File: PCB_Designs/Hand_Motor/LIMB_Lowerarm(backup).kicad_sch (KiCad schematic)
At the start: 18 parts, among them J1 Power In, J10 68800311622, J11 Servo Power, J12 68800611722, J13 68800611722, J2 IMU, J3 CAN IN, J4 CAN OUT, J5 68800311622, J6 68800311622, J7 68800311622, J8 68800311622, J9 68800311622, U1 ESP32-C3-Zero, U3 SN65HVD230

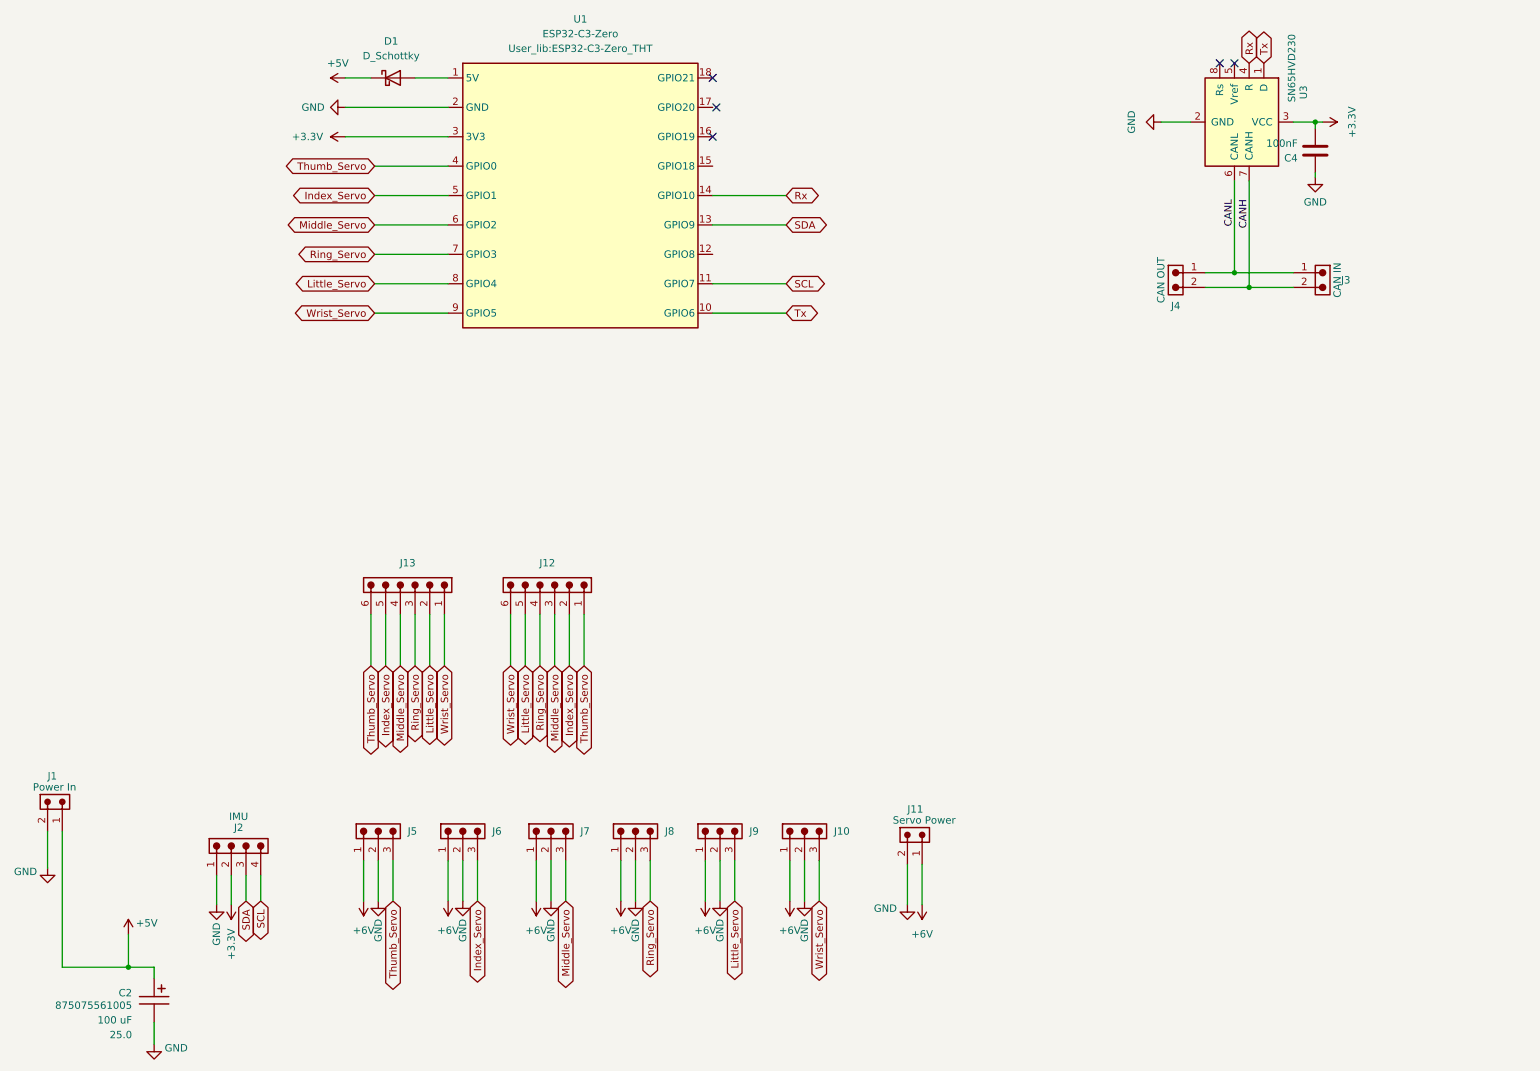
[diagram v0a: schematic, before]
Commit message: PCB kort
Uppdaterat Hand Pressure och Motor korten
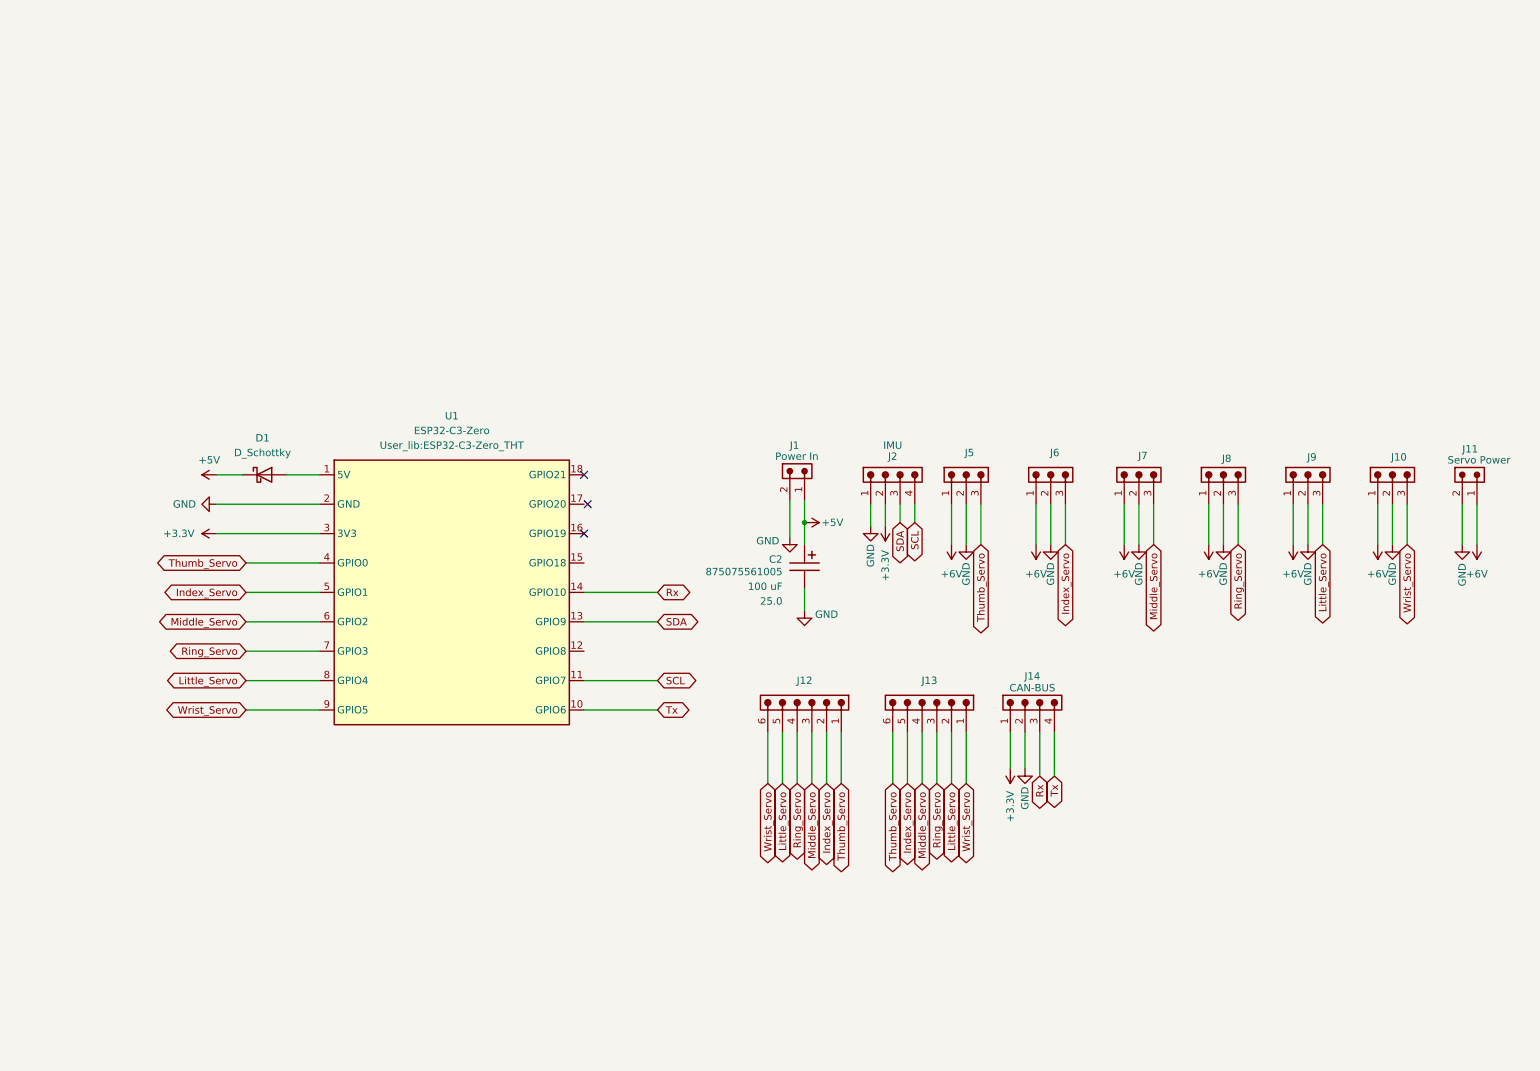
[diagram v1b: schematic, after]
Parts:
- removed C4: 100nF, Capacitor_SMD:C_0805_2012Metric_Pad1.18x1.45mm_HandSolder, symbol Device:C
- removed J3: CAN IN, Connector_THT_Wurth:J_Wurth_WR-WTB_68800211622, symbol Connector_Wurth_WR-WTB:68800211622
- removed J4: CAN OUT, Connector_THT_Wurth:J_Wurth_WR-WTB_68800211622, symbol Connector_Wurth_WR-WTB:68800211622
- removed U3: SN65HVD230, Package_SO:SOIC-8_3.9x4.9mm_P1.27mm, symbol Interface_CAN_LIN:SN65HVD230
- added J14: CAN-BUS, Connector_THT_Wurth:J_Wurth_WR-WTB_68800411622, symbol Connector_Wurth_WR-WTB:68800411622
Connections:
- net +3.3V: now also J14.1
- net GND: now also J14.2
- net Rx: now also J14.3
- net Tx: now also J14.4
- no-connect marks 5 -> 3
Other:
- moved on the sheet: C2, D1, J1, J10, J11, J12, J13, J2, J5, J6, J7, J8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
